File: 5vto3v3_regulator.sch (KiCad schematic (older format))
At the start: 11 parts

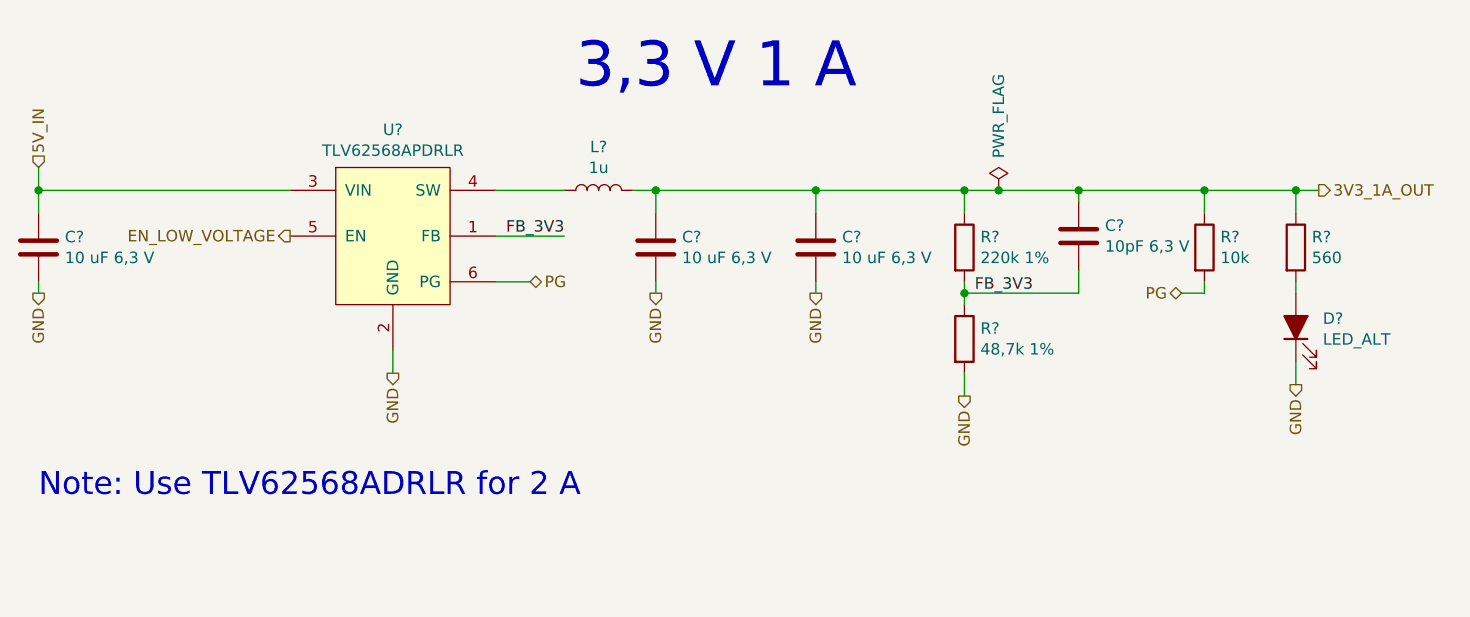
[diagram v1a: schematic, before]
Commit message: Schematic modified (Hierarchy) Bug where SPI was active when creset or ss was low fixed PCB layout started (almost all parts are at position) No parts on the bottom so far Arduino and PMOD header spacings corrected according to its standards
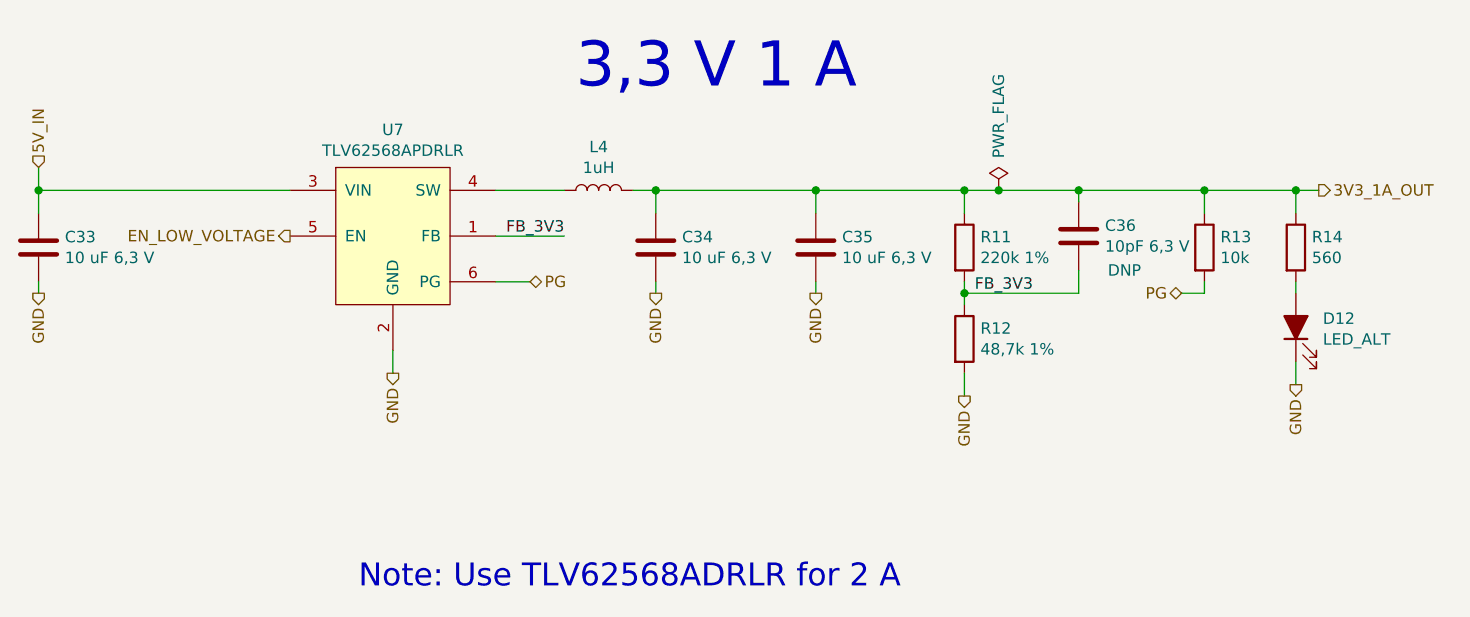
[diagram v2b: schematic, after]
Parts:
- C36: renamed from C?; DNP (none) -> DNP
- L4: renamed from L?; value 1u -> 1uH
- gave numbers to parts that had none: 9
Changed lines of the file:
@@
 $Descr A4 11693 8268
 encoding utf-8
-Sheet 6 7
+Sheet 6 14
 Title ""
 Date ""
@@
 P 2500 1750
 AR Path="/5ECD2614/5F6ECED9" Ref="U?"  Part="1"
-AR Path="/5ECD2614/5F6D5D15/5F6ECED9" Ref="U?"  Part="1"
-F 0 "U?" H 2500 2215 50  0000 C CNN
+AR Path="/5ECD2614/5F6D5D15/5F6ECED9" Ref="U7"  Part="1"
+F 0 "U7" H 2500 2215 50  0000 C CNN
 F 1 "TLV62568APDRLR" H 2500 2124 50  0000 C CNN
 F 2 "footprints:Texas_DRL_SOT-563_1.6x1.6mm_0.5mm-pitch_footprint" H 2500 1450 50  0001 C CNN
@@
 P 950 1800
 AR Path="/5ECD2614/5F6ECEE4" Ref="C?"  Part="1"
-AR Path="/5ECD2614/5F6D5D15/5F6ECEE4" Ref="C?"  Part="1"
-F 0 "C?" H 1065 1846 50  0000 L CNN
+AR Path="/5ECD2614/5F6D5D15/5F6ECEE4" Ref="C33"  Part="1"
+F 0 "C33" H 1065 1846 50  0000 L CNN
 F 1 "10 uF 6,3 V" H 1065 1755 50  0000 L CNN
 F 2 "Capacitor_SMD:C_0603_1608Metric" H 988 1650 50  0001 C CNN
@@
 P 3650 1800
 AR Path="/5ECD2614/5F6ECEEF" Ref="C?"  Part="1"
-AR Path="/5ECD2614/5F6D5D15/5F6ECEEF" Ref="C?"  Part="1"
-F 0 "C?" H 3765 1846 50  0000 L CNN
+AR Path="/5ECD2614/5F6D5D15/5F6ECEEF" Ref="C34"  Part="1"
+F 0 "C34" H 3765 1846 50  0000 L CNN
 F 1 "10 uF 6,3 V" H 3765 1755 50  0000 L CNN
 F 2 "Capacitor_SMD:C_0603_1608Metric" H 3688 1650 50  0001 C CNN
@@
 P 4350 1800
 AR Path="/5ECD2614/5F6ECEFA" Ref="C?"  Part="1"
-AR Path="/5ECD2614/5F6D5D15/5F6ECEFA" Ref="C?"  Part="1"
-F 0 "C?" H 4465 1846 50  0000 L CNN
+AR Path="/5ECD2614/5F6D5D15/5F6ECEFA" Ref="C35"  Part="1"
+F 0 "C35" H 4465 1846 50  0000 L CNN
 F 1 "10 uF 6,3 V" H 4465 1755 50  0000 L CNN
 F 2 "Capacitor_SMD:C_0603_1608Metric" H 4388 1650 50  0001 C CNN
@@
 P 5000 1800
 AR Path="/5ECD2614/5F6ECF05" Ref="R?"  Part="1"
-AR Path="/5ECD2614/5F6D5D15/5F6ECF05" Ref="R?"  Part="1"
-F 0 "R?" H 5070 1846 50  0000 L CNN
+AR Path="/5ECD2614/5F6D5D15/5F6ECF05" Ref="R11"  Part="1"
+F 0 "R11" H 5070 1846 50  0000 L CNN
 F 1 "220k 1%" H 5070 1755 50  0000 L CNN
 F 2 "Resistor_SMD:R_0603_1608Metric" V 4930 1800 50  0001 C CNN
@@
 P 5000 2200
 AR Path="/5ECD2614/5F6ECF10" Ref="R?"  Part="1"
-AR Path="/5ECD2614/5F6D5D15/5F6ECF10" Ref="R?"  Part="1"
-F 0 "R?" H 5070 2246 50  0000 L CNN
+AR Path="/5ECD2614/5F6D5D15/5F6ECF10" Ref="R12"  Part="1"
+F 0 "R12" H 5070 2246 50  0000 L CNN
 F 1 "48,7k 1%" H 5070 2155 50  0000 L CNN
 F 2 "Resistor_SMD:R_0603_1608Metric" V 4930 2200 50  0001 C CNN
@@
 P 3400 1550
 AR Path="/5ECD2614/5F6ECF44" Ref="L?"  Part="1"
-AR Path="/5ECD2614/5F6D5D15/5F6ECF44" Ref="L?"  Part="1"
-F 0 "L?" V 3590 1550 50  0000 C CNN
-F 1 "1u" V 3499 1550 50  0000 C CNN
+AR Path="/5ECD2614/5F6D5D15/5F6ECF44" Ref="L4"  Part="1"
+F 0 "L4" V 3590 1550 50  0000 C CNN
+F 1 "1uH" V 3499 1550 50  0000 C CNN
 F 2 "footprints:L_1008_2520Metric_2.5x2mm_footprint" H 3400 1550 50  0001 C CNN
 F 3 "https://www.yuden.co.jp/productdata/catalog/wound10_e.pdf" H 3400 1550 50  0001 C CNN
@@
 P 5500 1750
 AR Path="/5ECD2614/5F6ECF59" Ref="C?"  Part="1"
-AR Path="/5ECD2614/5F6D5D15/5F6ECF59" Ref="C?"  Part="1"
-F 0 "C?" H 5615 1796 50  0000 L CNN
+AR Path="/5ECD2614/5F6D5D15/5F6ECF59" Ref="C36"  Part="1"
+F 0 "C36" H 5615 1796 50  0000 L CNN
 F 1 "10pF 6,3 V" H 5615 1705 50  0000 L CNN
 F 2 "Capacitor_SMD:C_0603_1608Metric" H 5538 1600 50  0001 C CNN
@@
 F 7 "CL10C100JB8NNNC" H -250 -7550 50  0001 C CNN "Mfg Part Num"
 F 8 "Any" H -250 -7550 50  0001 C CNN "Spec"
+F 9 "DNP" H 5700 1600 50  0000 C CNN "DNP"
 	1    5500 1750
 	1    0    0    -1
@@
 P 5150 1550
 AR Path="/5ECD2614/5F6ECF63" Ref="#FLG?"  Part="1"
-AR Path="/5ECD2614/5F6D5D15/5F6ECF63" Ref="#FLG?"  Part="1"
-F 0 "#FLG?" H 5150 1625 50  0001 C CNN
+AR Path="/5ECD2614/5F6D5D15/5F6ECF63" Ref="#FLG07"  Part="1"
+F 0 "#FLG07" H 5150 1625 50  0001 C CNN
 F 1 "PWR_FLAG" V 5150 1875 50  0000 C CNN
 F 2 "" H 5150 1550 50  0001 C CNN
@@
 P 6050 1800
 AR Path="/5ECD2614/5F6ECF7B" Ref="R?"  Part="1"
-AR Path="/5ECD2614/5F6D5D15/5F6ECF7B" Ref="R?"  Part="1"
-F 0 "R?" H 6120 1846 50  0000 L CNN
+AR Path="/5ECD2614/5F6D5D15/5F6ECF7B" Ref="R13"  Part="1"
+F 0 "R13" H 6120 1846 50  0000 L CNN
 F 1 "10k" H 6120 1755 50  0000 L CNN
 F 2 "Resistor_SMD:R_0603_1608Metric" V 5980 1800 50  0001 C CNN
@@
 P 6450 2150
 AR Path="/5ECD2614/5F6ECF8A" Ref="D?"  Part="1"
-AR Path="/5ECD2614/5F6D5D15/5F6ECF8A" Ref="D?"  Part="1"
-F 0 "D?" V 6489 2032 50  0000 R CNN
+AR Path="/5ECD2614/5F6D5D15/5F6ECF8A" Ref="D12"  Part="1"
+F 0 "D12" V 6489 2032 50  0000 R CNN
 F 1 "LED_ALT" V 6398 2032 50  0000 R CNN
 F 2 "LED_SMD:LED_0603_1608Metric" H 6450 2150 50  0001 C CNN
@@
 P 6450 1800
 AR Path="/5ECD2614/5F6ECF9C" Ref="R?"  Part="1"
-AR Path="/5ECD2614/5F6D5D15/5F6ECF9C" Ref="R?"  Part="1"
-F 0 "R?" H 6520 1846 50  0000 L CNN
+AR Path="/5ECD2614/5F6D5D15/5F6ECF9C" Ref="R14"  Part="1"
+F 0 "R14" H 6520 1846 50  0000 L CNN
 F 1 "560" H 6520 1755 50  0000 L CNN
 F 2 "Resistor_SMD:R_0603_1608Metric" V 6380 1800 50  0001 C CNN
@@
 Wire Wire Line
 	950  1550 2050 1550
-Text Notes 950  2900 0    100  ~ 0
+Text Notes 2350 3300 0    100  ~ 0
 Note: Use TLV62568ADRLR for 2 A
 Text HLabel 950  1450 1    50   Input ~ 0
